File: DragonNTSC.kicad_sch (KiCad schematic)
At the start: 19 parts, among them IC1 74LS273N, IC2 MC6847, IC3 MC1372, J2 Board Interconnect Male, J2 Video Output, Q161 2N4403, Q162 2N4401

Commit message: prepare alpha2 build
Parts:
- added C5: 150pF, Capacitor_THT:C_Rect_L7.0mm_W2.5mm_P5.00mm, symbol Device:C_Small
- added C6: 0.1uF, Capacitor_THT:C_Rect_L7.0mm_W2.5mm_P5.00mm, symbol Device:C_Small
- added FB1: ?uH, Inductor_THT:L_Axial_L7.0mm_D3.3mm_P5.08mm_Vertical_Fastron_MICC, symbol Device:FerriteBead_Small
- added R7: 150R, Resistor_THT:R_Axial_DIN0207_L6.3mm_D2.5mm_P2.54mm_Vertical, symbol Device:R_Small
- added R8: 10k, Resistor_THT:R_Axial_DIN0207_L6.3mm_D2.5mm_P2.54mm_Vertical, symbol Device:R_Small
- C11: value 1uF -> 10uF
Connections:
- net CHB: now also C6.2
- net GND: now also C5.1, C6.1
- net LUM: now also C5.2
- net VCLK: now also FB1.2, R7.1, R8.1; no longer IC2.33 (CLK), IC3.2 (OSC), J2.18 (Pin_18)
- net at C164.2: now also RV161.2; no longer RV161.1
- net D4: now reaches IC1.12 (Q4), IC2.7 (D4)
- net D5: now reaches IC1.15 (Q5), IC2.8 (D5)
- net D6: now reaches IC1.16 (Q6), IC2.2 (D6), IC2.32 (INV)
- net D7: now reaches IC1.19 (Q7), IC2.34 (~{A}/S), IC2.40 (D7)
- net D0: now reaches IC1.2 (Q0), IC2.3 (D0)
- net D1: now reaches IC1.5 (Q1), IC2.4 (D1)
- net D2: now reaches IC1.6 (Q2), IC2.5 (D2)
- net D3: now reaches IC1.9 (Q3), IC2.6 (D3)
- new net: IC3.2 (OSC), R8.2
- new net: FB1.1, J2.18 (Pin_18)
- new net: IC2.33 (CLK), R7.2
- no-connect marks 17 -> 18
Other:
- moved on the sheet: Q162

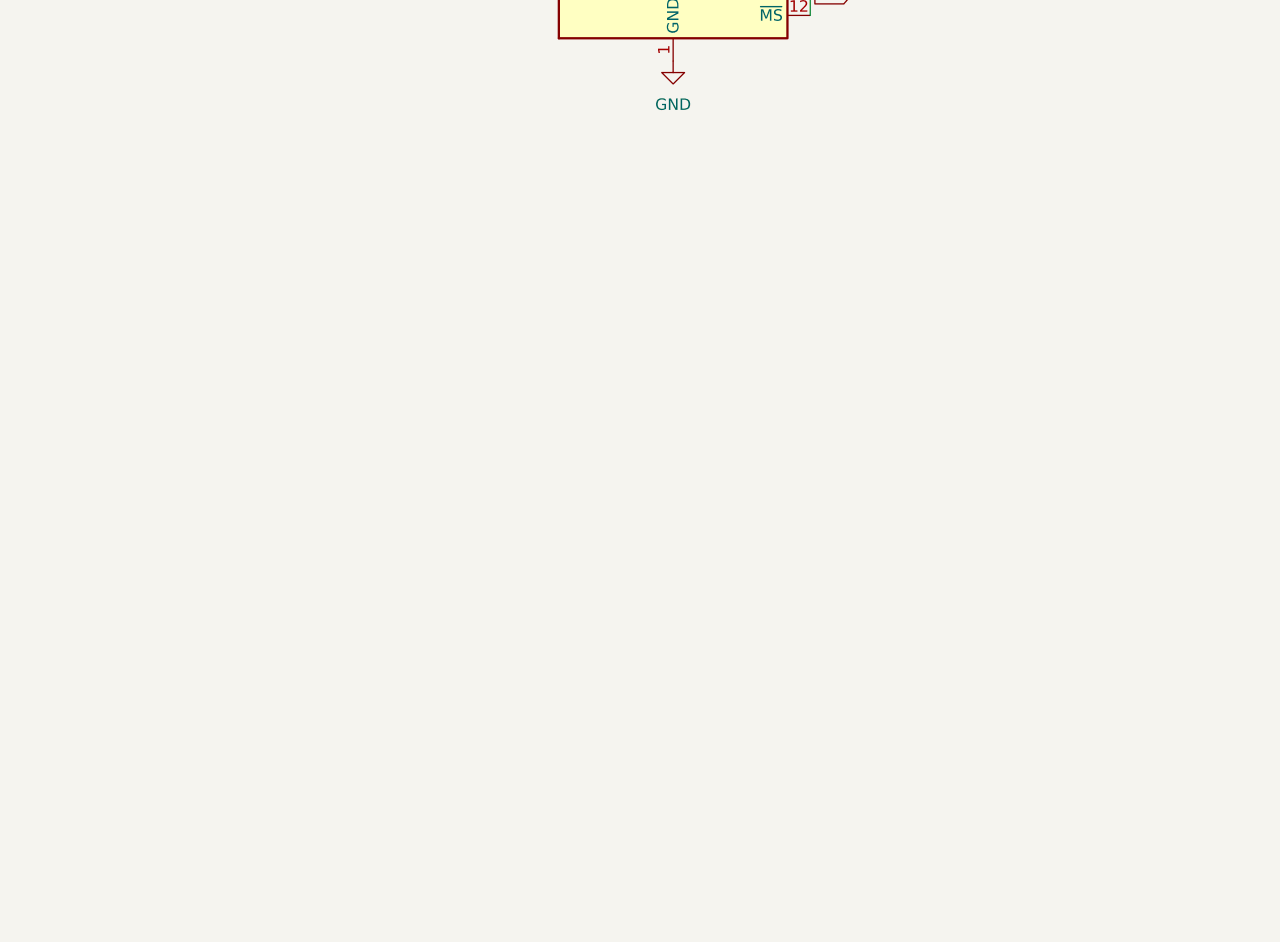
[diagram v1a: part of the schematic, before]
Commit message: add 555 timer
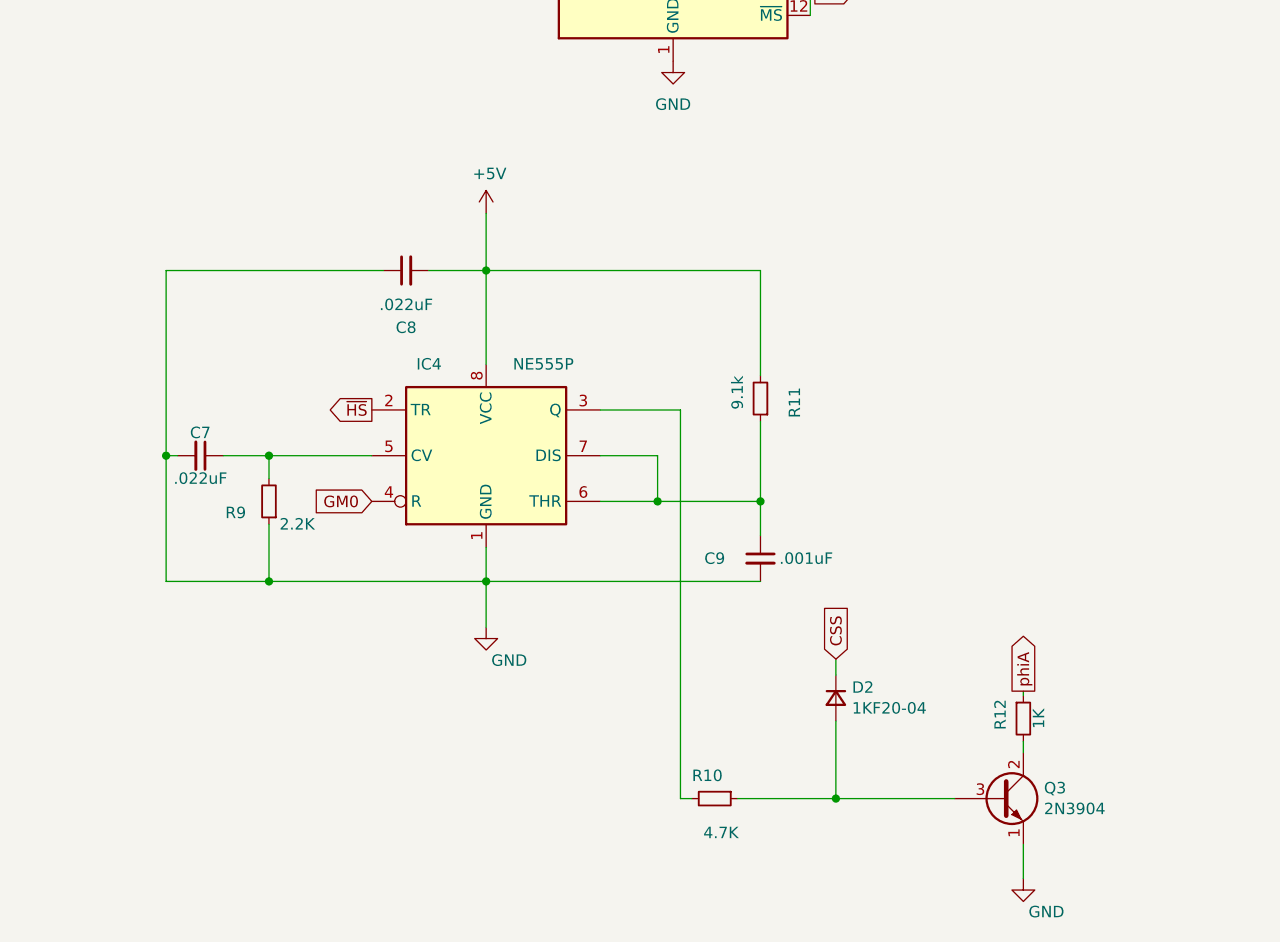
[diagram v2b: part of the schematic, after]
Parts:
- added C7, C8: .022uF, Capacitor_THT:C_Disc_D8.0mm_W2.5mm_P5.00mm, symbol Device:C_Small
- added C9: .001uF, Capacitor_THT:C_Rect_L4.0mm_W2.5mm_P2.50mm, symbol Device:C_Small
- added D2: 1KF20-04, Diode_THT:D_A-405_P10.16mm_Horizontal, symbol Device:D_Small
- added IC4: NE555P, Package_DIP:DIP-8_W7.62mm, symbol Timer:NE555P
- added Q3: 2N3904, Package_TO_SOT_THT:TO-92_Inline, symbol Device:Q_NPN_ECB
- added R10: 4.7K, Resistor_THT:R_Axial_DIN0207_L6.3mm_D2.5mm_P2.54mm_Vertical, symbol Device:R_Small
- added R11: 9.1k, Resistor_THT:R_Axial_DIN0207_L6.3mm_D2.5mm_P2.54mm_Vertical, symbol Device:R_Small
- added R12: 1K, Resistor_THT:R_Axial_DIN0207_L6.3mm_D2.5mm_P2.54mm_Vertical, symbol Device:R_Small
- added R9: 2.2K, Resistor_THT:R_Axial_DIN0207_L6.3mm_D2.5mm_P2.54mm_Vertical, symbol Device:R_Small
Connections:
- net +5V: now also C8.2, IC4.8 (VCC), R11.2
- net CSS: now also D2.1 (K)
- net GM0: now also IC4.4 (R)
- net GND: now also C7.2, C8.1, C9.2, IC4.1 (GND), Q3.1 (E), R9.1
- net phiA: now also R12.1
- net ~{HS}: now also IC4.2 (TR)
- new net: D2.2 (A), Q3.3 (B), R10.1
- new net: C9.1, IC4.6 (THR), IC4.7 (DIS), R11.1
- new net: IC4.3 (Q), R10.2
- new net: C7.1, IC4.5 (CV), R9.2
- new net: Q3.2 (C), R12.2
